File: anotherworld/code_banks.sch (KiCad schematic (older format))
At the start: 3 parts

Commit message: lots of stuff :-)
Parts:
- added U?: 27C801, ~, symbol 27C801
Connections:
- net DATA_0: now also U?.13 (D0); no longer U?.3 (D0), U?.3 (D0)
- net DATA_1: now also U?.14 (D1); no longer U?.4 (D1), U?.4 (D1)
- net DATA_2: now also U?.15 (D2); no longer U?.7 (D2), U?.7 (D2)
- net DATA_3: now also U?.17 (D3); no longer U?.8 (D3), U?.8 (D3)
- net DATA_4: now also U?.18 (D4); no longer U?.12 (O4), U?.13 (D4), U?.13 (D4)
- net DATA_5: now also U?.19 (D5); no longer U?.14 (D5), U?.14 (D5), U?.15 (O5)
- net DATA_6: now also U?.20 (D6); no longer U?.16 (O6), U?.17 (D6), U?.17 (D6)
- net DATA_7: now also U?.21 (D7); no longer U?.18 (D7), U?.18 (D7), U?.19 (O7)
- net GND: now also U?.16 (GND)
- net VCC: now also U?.32 (VCC)
- net at U?.3 (D0): now also U?.2 (A16)
- net at U?.4 (D1): now also U?.30 (A17)
- net at U?.7 (D2): now also U?.31 (A18)
- net at U?.8 (D3): now also U?.1 (A19)
- net CODEBANK_REG_CLK renamed CODEBANK_CLK
- new net: U?.10 (A2), U?.7 (D2)
- new net: U?.11 (A1), U?.4 (D1)
- new net: U?.12 (A0), U?.3 (D0)
- new net: U?.23 (A10), U?.7 (D2)
- new net: U?.25 (A11), U?.8 (D3)
- new net: U?.26 (A9), U?.4 (D1)
- new net: U?.27 (A8), U?.3 (D0)
- new net: U?.14 (D5), U?.28 (A13)
- new net: U?.17 (D6), U?.29 (A14)
- new net: U?.18 (D7), U?.3 (A15)
- new net: U?.13 (D4), U?.4 (A12)
- new net: U?.18 (D7), U?.5 (A7)
- new net: U?.17 (D6), U?.6 (A6)
- new net: U?.14 (D5), U?.7 (A5)
- new net: U?.13 (D4), U?.8 (A4)
- new net: U?.8 (D3), U?.9 (A3)
- new net -CODEROM_OE: U?.22 (E)
- no-connect marks 0 -> 9
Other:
- moved on the sheet: U?

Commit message: wondering about the microcode signaling...
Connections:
- net -IPH_OE is gone; now on net GND: U?.1 (OE)
- net -IPL_OE is gone; now on net GND: U?.1 (OE)
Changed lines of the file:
@@
 $Descr A3 16535 11693
 encoding utf-8
-Sheet 8 8
+Sheet 7 8
 Title ""
 Date "8 aug 2016"
@@
 Connection ~ 8300 2600
 Connection ~ 8400 2750
-Text GLabel 5200 5100 0    60   Input ~ 0
--IPH_OE
-Wire Wire Line
-	7400 4300 7400 5100
-Wire Wire Line
-	7400 5100 5200 5100
+Wire Wire Line
+	7400 4300 7400 4400
 Text GLabel 5200 4750 0    60   Input ~ 0
 IPH_CLK
@@
 Wire Wire Line
 	7500 4750 5200 4750
-Text GLabel 5200 5250 0    60   Input ~ 0
--IPL_OE
 Text GLabel 5200 4900 0    60   Input ~ 0
 IPL_CLK
@@
 $EndComp
 Wire Wire Line
-	8700 4300 8700 5250
-Wire Wire Line
-	8700 5250 5200 5250
+	8700 4300 8700 4400
 $Comp
 L 74LS374 U?
@@
 Wire Wire Line
 	8800 4900 8800 4300
+$Comp
+L GND #PWR?
+U 1 1 57A7F509
+P 7400 4400
+F 0 "#PWR?" H 7400 4400 30  0001 C CNN
+F 1 "GND" H 7400 4330 30  0001 C CNN
+F 2 "" H 7400 4400 60  0000 C CNN
+F 3 "" H 7400 4400 60  0000 C CNN
+	1    7400 4400
+	1    0    0    -1
+$EndComp
+$Comp
+L GND #PWR?
+U 1 1 57A7F50F
+P 8700 4400
+F 0 "#PWR?" H 8700 4400 30  0001 C CNN
+F 1 "GND" H 8700 4330 30  0001 C CNN
+F 2 "" H 8700 4400 60  0000 C CNN
+F 3 "" H 8700 4400 60  0000 C CNN
+	1    8700 4400
+	1    0    0    -1
+$EndComp
 $EndSCHEMATC

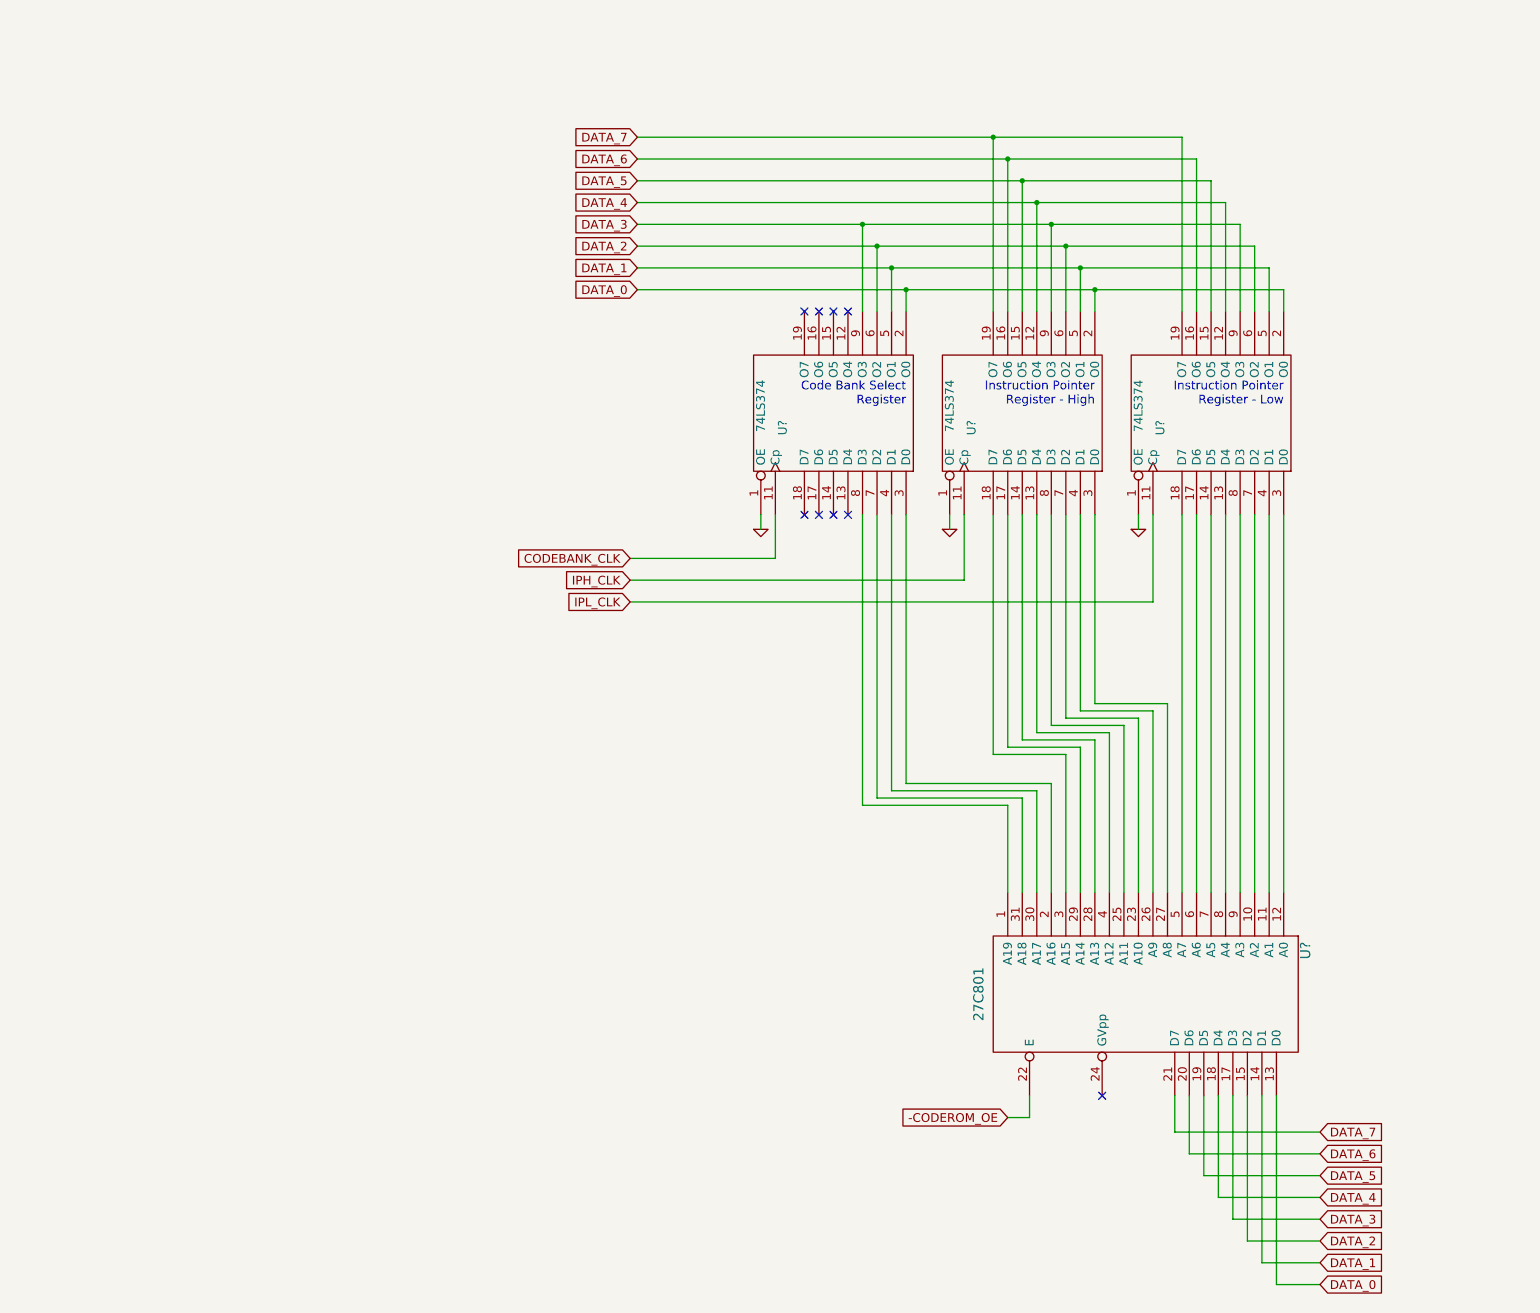
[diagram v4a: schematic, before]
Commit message: palette selection and video output circuitry (Color DAC and Palette ROM)
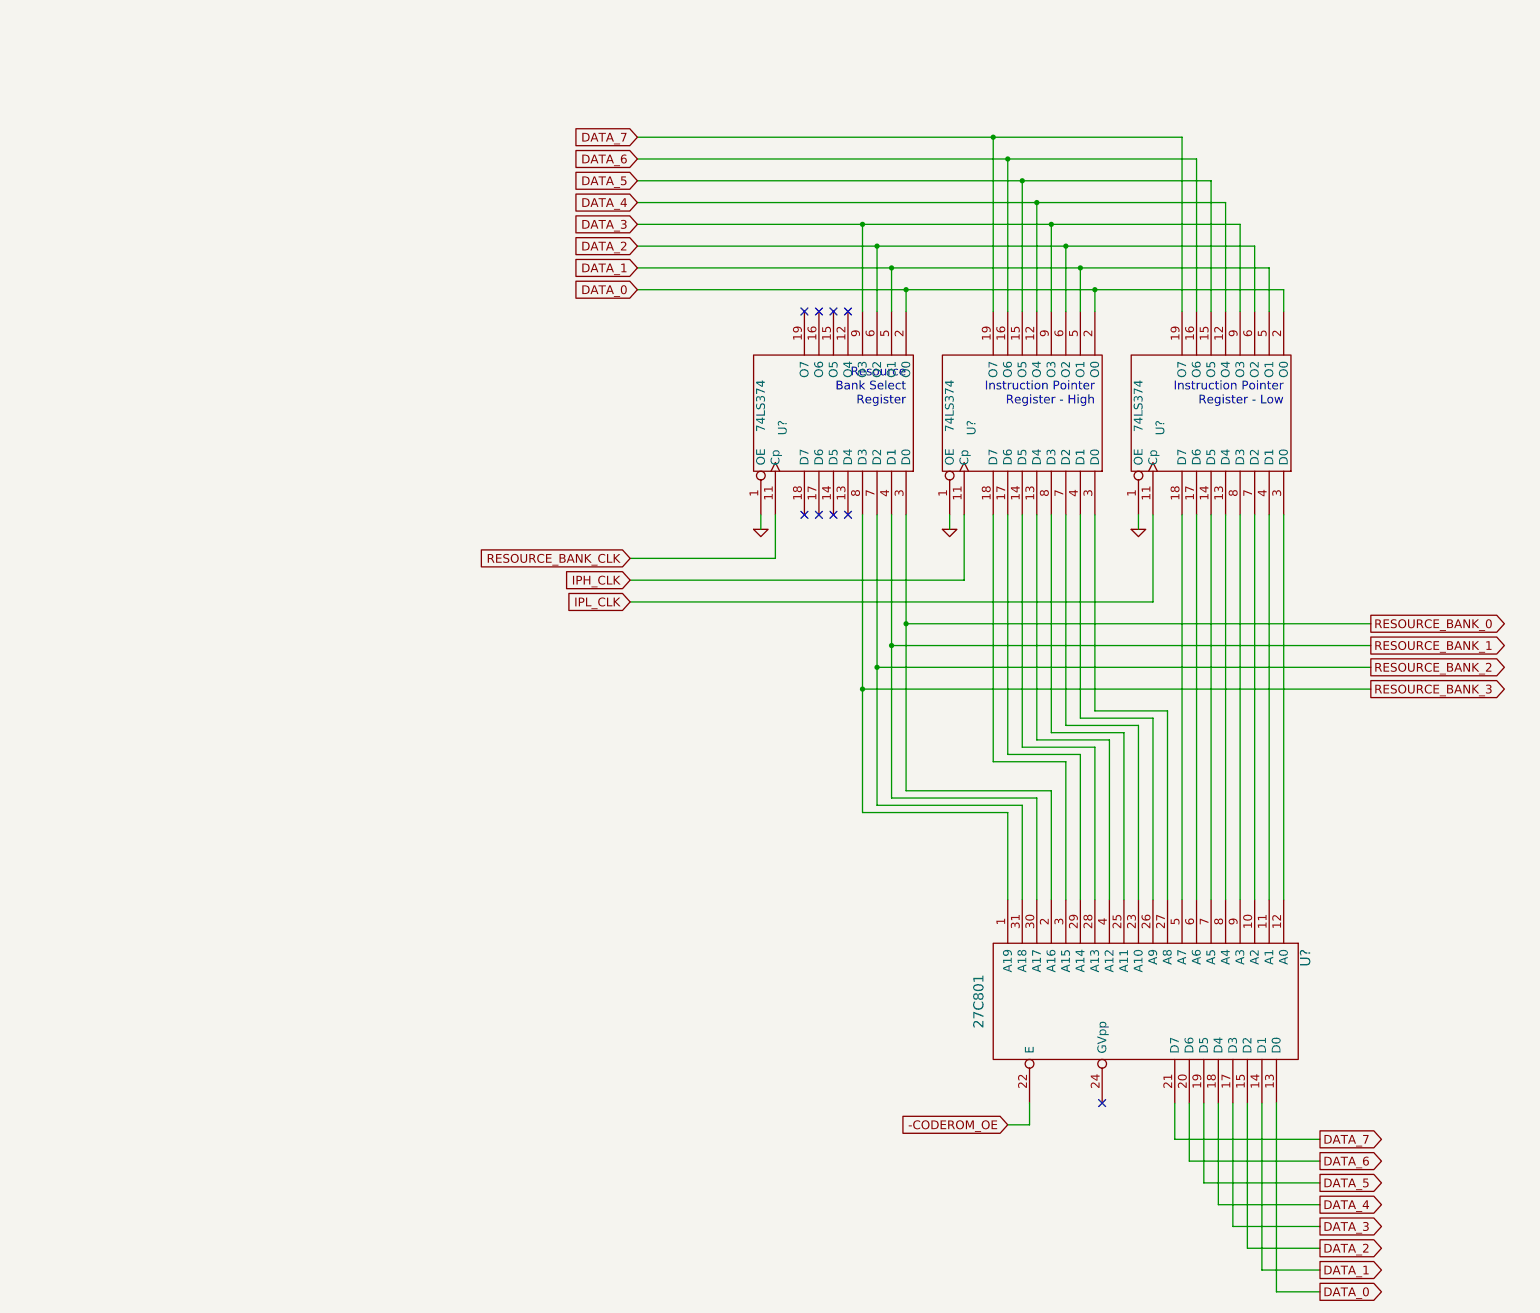
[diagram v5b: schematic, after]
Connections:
- net RESOURCE_BANK_3: now reaches U?.1 (A19), U?.8 (D3)
- net RESOURCE_BANK_0: now reaches U?.2 (A16), U?.3 (D0)
- net RESOURCE_BANK_1: now reaches U?.30 (A17), U?.4 (D1)
- net RESOURCE_BANK_2: now reaches U?.31 (A18), U?.7 (D2)
- net CODEBANK_CLK renamed RESOURCE_BANK_CLK
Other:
- note added: "Resource\nBank Select\nRegister"
- note removed: "Code Bank Select\nRegister"
- moved on the sheet: U?
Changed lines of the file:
@@
 $Descr A3 16535 11693
 encoding utf-8
-Sheet 7 7
+Sheet 7 8
 Title ""
-Date "9 aug 2016"
+Date "10 aug 2016"
 Rev ""
 Comp ""
@@
 $EndComp
 Text Notes 7100 3550 2    60   ~ 0
-Code Bank Select\nRegister
+Resource\nBank Select\nRegister
 $Comp
 L GND #PWR?
@@
 	6100 4300 6100 4400
 Text GLabel 5200 4600 0    60   Input ~ 0
-CODEBANK_CLK
+RESOURCE_BANK_CLK
 Wire Wire Line
 	5200 4600 6200 4600
@@
 L 27C801 U?
 U 1 1 57A7D10C
-P 8800 7600
-F 0 "U?" H 8500 8650 70  0000 C CNN
-F 1 "27C801" H 8800 6400 70  0000 C CNN
-F 2 "~" H 8800 7600 60  0000 C CNN
-F 3 "~" H 8800 7600 60  0000 C CNN
-	1    8800 7600
+P 8800 7650
+F 0 "U?" H 8500 8700 70  0000 C CNN
+F 1 "27C801" H 8800 6450 70  0000 C CNN
+F 2 "~" H 8800 7650 60  0000 C CNN
+F 3 "~" H 8800 7650 60  0000 C CNN
+	1    8800 7650
 	0    1    1    0
 $EndComp
 Wire Wire Line
-	9700 4300 9700 6900
-Wire Wire Line
-	9600 6900 9600 4300
-Wire Wire Line
-	9500 4300 9500 6900
-Wire Wire Line
-	9400 6900 9400 4300
-Wire Wire Line
-	9300 4300 9300 6900
-Wire Wire Line
-	9200 6900 9200 4300
-Wire Wire Line
-	9100 4300 9100 6900
-Wire Wire Line
-	9000 6900 9000 4300
-Wire Wire Line
-	8900 6900 8900 5600
-Wire Wire Line
-	8900 5600 8400 5600
-Wire Wire Line
-	8400 5600 8400 4300
-Wire Wire Line
-	8300 4300 8300 5650
-Wire Wire Line
-	8300 5650 8800 5650
-Wire Wire Line
-	8800 5650 8800 6900
-Wire Wire Line
-	8700 6900 8700 5700
-Wire Wire Line
-	8700 5700 8200 5700
-Wire Wire Line
-	8200 5700 8200 4300
-Wire Wire Line
-	8100 4300 8100 5750
-Wire Wire Line
-	8100 5750 8600 5750
-Wire Wire Line
-	8600 5750 8600 6900
-Wire Wire Line
-	8500 6900 8500 5800
-Wire Wire Line
-	8500 5800 8000 5800
-Wire Wire Line
-	8000 5800 8000 4300
-Wire Wire Line
-	7900 4300 7900 5850
-Wire Wire Line
-	7900 5850 8400 5850
-Wire Wire Line
-	8400 5850 8400 6900
-Wire Wire Line
-	8300 6900 8300 5900
-Wire Wire Line
-	8300 5900 7800 5900
-Wire Wire Line
-	7800 5900 7800 4300
-Wire Wire Line
-	7700 4300 7700 5950
-Wire Wire Line
-	7700 5950 8200 5950
-Wire Wire Line
-	8200 5950 8200 6900
-Wire Wire Line
-	8100 6900 8100 6150
-Wire Wire Line
-	8100 6150 7100 6150
-Wire Wire Line
-	7100 6150 7100 4300
-Wire Wire Line
-	7000 4300 7000 6200
-Wire Wire Line
-	7000 6200 8000 6200
-Wire Wire Line
-	8000 6200 8000 6900
-Wire Wire Line
-	7900 6900 7900 6250
-Wire Wire Line
-	7900 6250 6900 6250
-Wire Wire Line
-	6900 6250 6900 4300
-Wire Wire Line
-	6800 4300 6800 6300
-Wire Wire Line
-	6800 6300 7800 6300
-Wire Wire Line
-	7800 6300 7800 6900
+	9700 4300 9700 6950
+Wire Wire Line
+	9600 6950 9600 4300
+Wire Wire Line
+	9500 4300 9500 6950
+Wire Wire Line
+	9400 6950 9400 4300
+Wire Wire Line
+	9300 4300 9300 6950
+Wire Wire Line
+	9200 6950 9200 4300
+Wire Wire Line
+	9100 4300 9100 6950
+Wire Wire Line
+	9000 6950 9000 4300
+Wire Wire Line
+	8900 6950 8900 5650
+Wire Wire Line
+	8900 5650 8400 5650
+Wire Wire Line
+	8400 5650 8400 4300
+Wire Wire Line
+	8300 4300 8300 5700
+Wire Wire Line
+	8300 5700 8800 5700
+Wire Wire Line
+	8800 5700 8800 6950
+Wire Wire Line
+	8700 6950 8700 5750
+Wire Wire Line
+	8700 5750 8200 5750
+Wire Wire Line
+	8200 5750 8200 4300
+Wire Wire Line
+	8100 4300 8100 5800
+Wire Wire Line
+	8100 5800 8600 5800
+Wire Wire Line
+	8600 5800 8600 6950
+Wire Wire Line
+	8500 6950 8500 5850
+Wire Wire Line
+	8500 5850 8000 5850
+Wire Wire Line
+	8000 5850 8000 4300
+Wire Wire Line
+	7900 4300 7900 5900
+Wire Wire Line
+	7900 5900 8400 5900
+Wire Wire Line
+	8400 5900 8400 6950
+Wire Wire Line
+	8300 6950 8300 5950
+Wire Wire Line
+	8300 5950 7800 5950
+Wire Wire Line
+	7800 5950 7800 4300
+Wire Wire Line
+	7700 4300 7700 6000
+Wire Wire Line
+	7700 6000 8200 6000
+Wire Wire Line
+	8200 6000 8200 6950
+Wire Wire Line
+	8100 6950 8100 6200
+Wire Wire Line
+	8100 6200 7100 6200
+Wire Wire Line
+	7000 6250 8000 6250
+Wire Wire Line
+	8000 6250 8000 6950
+Wire Wire Line
+	7900 6950 7900 6300
+Wire Wire Line
+	7900 6300 6900 6300
+Wire Wire Line
+	6800 6350 7800 6350
+Wire Wire Line
+	7800 6350 7800 6950
 NoConn ~ 6700 4300
 NoConn ~ 6600 4300
@@
 NoConn ~ 6500 2900
 NoConn ~ 6400 2900
-Text GLabel 9950 9600 2    60   Input ~ 0
+Text GLabel 9950 9650 2    60   Output ~ 0
 DATA_0
-Text GLabel 9950 9450 2    60   Input ~ 0
+Text GLabel 9950 9500 2    60   Output ~ 0
 DATA_1
-Text GLabel 9950 9300 2    60   Input ~ 0
+Text GLabel 9950 9350 2    60   Output ~ 0
 DATA_2
-Text GLabel 9950 9150 2    60   Input ~ 0
+Text GLabel 9950 9200 2    60   Output ~ 0
 DATA_3
-Text GLabel 9950 9000 2    60   Input ~ 0
+Text GLabel 9950 9050 2    60   Output ~ 0
 DATA_4
-Text GLabel 9950 8850 2    60   Input ~ 0
+Text GLabel 9950 8900 2    60   Output ~ 0
 DATA_5
-Text GLabel 9950 8700 2    60   Input ~ 0
+Text GLabel 9950 8750 2    60   Output ~ 0
 DATA_6
-Text GLabel 9950 8550 2    60   Input ~ 0
+Text GLabel 9950 8600 2    60   Output ~ 0
 DATA_7
 Wire Wire Line
-	8950 8300 8950 8550
-Wire Wire Line
-	8950 8550 9950 8550
-Wire Wire Line
-	9050 8300 9050 8700
-Wire Wire Line
-	9050 8700 9950 8700
-Wire Wire Line
-	9150 8300 9150 8850
-Wire Wire Line
-	9150 8850 9950 8850
-Wire Wire Line
-	9250 8300 9250 9000
-Wire Wire Line
-	9250 9000 9950 9000
-Wire Wire Line
-	9350 8300 9350 9150
-Wire Wire Line
-	9350 9150 9950 9150
-Wire Wire Line
-	9450 8300 9450 9300
-Wire Wire Line
-	9450 9300 9950 9300
-Wire Wire Line
-	9950 9450 9550 9450
-Wire Wire Line
-	9550 9450 9550 8300
-Wire Wire Line
-	9650 8300 9650 9600
-Wire Wire Line
-	9650 9600 9950 9600
-NoConn ~ 8450 8300
-Text GLabel 7800 8450 0    60   Input ~ 0
+	8950 8350 8950 8600
+Wire Wire Line
+	8950 8600 9950 8600
+Wire Wire Line
+	9050 8350 9050 8750
+Wire Wire Line
+	9050 8750 9950 8750
+Wire Wire Line
+	9150 8350 9150 8900
+Wire Wire Line
+	9150 8900 9950 8900
+Wire Wire Line
+	9250 8350 9250 9050
+Wire Wire Line
+	9250 9050 9950 9050
+Wire Wire Line
+	9350 8350 9350 9200
+Wire Wire Line
+	9350 9200 9950 9200
+Wire Wire Line
+	9450 8350 9450 9350
+Wire Wire Line
+	9450 9350 9950 9350
+Wire Wire Line
+	9950 9500 9550 9500
+Wire Wire Line
+	9550 9500 9550 8350
+Wire Wire Line
+	9650 8350 9650 9650
+Wire Wire Line
+	9650 9650 9950 9650
+NoConn ~ 8450 8350
+Text GLabel 7800 8500 0    60   Input ~ 0
 -CODEROM_OE
 Wire Wire Line
-	7800 8450 7950 8450
-Wire Wire Line
-	7950 8450 7950 8300
+	7800 8500 7950 8500
+Wire Wire Line
+	7950 8500 7950 8350
 Wire Wire Line
 	5200 4900 8800 4900
@@
 	1    0    0    -1
 $EndComp
+Text GLabel 10300 5050 2    60   Output ~ 0
+RESOURCE_BANK_0
+Text GLabel 10300 5200 2    60   Output ~ 0
+RESOURCE_BANK_1
+Text GLabel 10300 5350 2    60   Output ~ 0
+RESOURCE_BANK_2
+Text GLabel 10300 5500 2    60   Output ~ 0
+RESOURCE_BANK_3
+Wire Wire Line
+	7100 5050 10300 5050
+Wire Wire Line
+	7000 5200 10300 5200
+Wire Wire Line
+	6900 5350 10300 5350
+Wire Wire Line
+	6800 5500 10300 5500
+Connection ~ 7100 5050
+Connection ~ 7000 5200
+Connection ~ 6900 5350
+Connection ~ 6800 5500
+Wire Wire Line
+	7100 6200 7100 5050
+Wire Wire Line
+	7100 5050 7100 4300
+Wire Wire Line
+	7000 4300 7000 5200
+Wire Wire Line
+	7000 5200 7000 6250
+Wire Wire Line
+	6900 6300 6900 5350
+Wire Wire Line
+	6900 5350 6900 4300
+Wire Wire Line
+	6800 4300 6800 5500
+Wire Wire Line
+	6800 5500 6800 6350
 $EndSCHEMATC
